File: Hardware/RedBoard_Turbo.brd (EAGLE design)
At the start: 58.4 x 53.3 mm, 144 parts, among them Q1 2.5A/30V, Q2 2N7002PW, U1 MCP73831, U2 74AHC1G125, U3 3.3V, U4 ATSAMD21G-A, U5 W25Q32FV, Y1 32.768kHz

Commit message: Added board title
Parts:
- added U$84: (no value), buzzard_labels (28):REDBOARD_TURBO0
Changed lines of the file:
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@@
 <element name="FID3" library="SparkFun-Aesthetics" package="FIDUCIAL-1X2" value="FIDUCIAL1X2" x="12.7" y="5.08" rot="MR0"/>
 <element name="FID4" library="SparkFun-Aesthetics" package="FIDUCIAL-1X2" value="FIDUCIAL1X2" x="50.8" y="43.18" rot="MR0"/>
+<element name="U$84" library="buzzard_labels (28)" package="REDBOARD_TURBO0" value="" x="12.319" y="24.13"/>
 </elements>
 <signals>

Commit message: Add testpoint and label for LED
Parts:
- added TP1: TEST-POINTTP_15TH_THRU, SparkFun-Connectors:TP_15TH
- added U$85: (no value), buzzard_labels (31):400
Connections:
- net RX_LED/SWDIO: now also TP1.P$1
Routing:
- net RX_LED/SWDIO: track 69.2 -> 71.4 mm
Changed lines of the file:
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@@
 <wire x1="53.086" y1="53.34" x2="-1.27" y2="53.34" width="0.2032" layer="20"/>
 <text x="3.81" y="48.26" size="1.016" layer="16" font="vector" ratio="15" rot="MR0" align="top-center">v01</text>
-<dimension x1="0" y1="0" x2="57.15" y2="5.08" x3="28.575" y3="-20.32" textsize="1.27" textratio="15" layer="47" dtype="horizontal" unit="inch" precision="3"/>
 <dimension x1="0" y1="0" x2="54.61" y2="7.62" x3="-5.08" y3="3.81" textsize="1.27" textratio="15" layer="47" dtype="vertical" unit="inch"/>
 <dimension x1="0" y1="0" x2="54.61" y2="35.56" x3="-7.62" y3="17.78" textsize="1.27" textratio="15" layer="47" dtype="vertical" unit="inch"/>
-<dimension x1="0" y1="0" x2="3.81" y2="50.8" x3="1.905" y3="-5.08" textsize="1.27" textratio="15" layer="47" dtype="horizontal" unit="inch" precision="3"/>
-<dimension x1="0" y1="0" x2="2.54" y2="2.54" x3="1.27" y3="-2.54" textsize="1.27" textratio="15" layer="47" dtype="horizontal" unit="inch" precision="3"/>
 <dimension x1="0" y1="0" x2="0" y2="53.34" x3="-12.7" y3="26.67" textsize="1.27" textratio="15" layer="47" dtype="vertical" unit="inch"/>
-<dimension x1="0" y1="0" x2="54.61" y2="35.56" x3="27.305" y3="-17.78" textsize="1.27" textratio="15" layer="47" dtype="horizontal" unit="inch" precision="3"/>
 <text x="34.29" y="-29.21" size="1.778" layer="51" font="vector" ratio="15">Jim Lindblom</text>
 <text x="44.958" y="46.609" size="1.27" layer="21" font="vector" ratio="15" rot="R90" align="center-right">~</text>
@@
 <text x="43.942" y="46.99" size="1.27" layer="22" font="vector" ratio="15" rot="MR90" align="center-right">~</text>
 <text x="-17.78" y="-8.89" size="1.27" layer="47" font="vector" ratio="15">Units in inches</text>
-<dimension x1="0" y1="0" x2="16.51" y2="2.54" x3="8.255" y3="-7.62" textsize="1.27" textratio="15" layer="47" dtype="horizontal" unit="inch" precision="3"/>
-<dimension x1="0" y1="0" x2="39.37" y2="2.54" x3="19.685" y3="-15.24" textsize="1.27" textratio="15" layer="47" dtype="horizontal" unit="inch" precision="3"/>
 <dimension x1="0" y1="0" x2="16.51" y2="2.54" x3="-1.27" y3="1.27" textsize="1.27" textratio="15" layer="47" dtype="vertical" unit="inch" precision="3"/>
 <dimension x1="0" y1="0" x2="7.366" y2="50.8" x3="-10.16" y3="25.4" textsize="1.27" textratio="15" layer="47" dtype="vertical" unit="inch" precision="3"/>
-<dimension x1="0" y1="0" x2="7.366" y2="50.8" x3="3.683" y3="-10.16" textsize="1.27" textratio="15" layer="47" dtype="horizontal" unit="inch" precision="3"/>
-<dimension x1="0" y1="0" x2="34.29" y2="50.8" x3="17.145" y3="-12.7" textsize="1.27" textratio="15" layer="47" dtype="horizontal" unit="inch" precision="3"/>
+<dimension x1="-1.27" y1="0" x2="2.54" y2="2.54" x3="0.635" y3="-3.81" textsize="1.27" textratio="15" layer="47" dtype="horizontal" unit="inch"/>
 </plain>
 <attributes>
@@
 <element name="FID4" library="SparkFun-Aesthetics" package="FIDUCIAL-1X2" value="FIDUCIAL1X2" x="50.8" y="43.18" rot="MR0"/>
 <element name="U$84" library="buzzard_labels (28)" package="REDBOARD_TURBO0" value="" x="12.319" y="24.13"/>
+<element name="TP1" library="SparkFun-Connectors" package="TP_15TH" value="TEST-POINTTP_15TH_THRU" x="41.275" y="19.685"/>
+<element name="U$85" library="buzzard_labels (31)" package="400" value="" x="34.163" y="40.132" rot="R90"/>
 </elements>
 <signals>
@@
 <wire x1="39.751" y1="18.161" x2="39.497" y2="18.415" width="0.2032" layer="1"/>
 <wire x1="39.497" y1="18.415" x2="38.735" y2="18.415" width="0.2032" layer="1"/>
+<contactref element="TP1" pad="P$1"/>
+<wire x1="39.751" y1="18.161" x2="41.275" y2="19.685" width="0.254" layer="1"/>
 </signal>
 <signal name="TX_LED">

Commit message: Changes from review
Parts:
- moved C11 1.27 mm to (33.0, 26.7)
- moved C3 1.27 mm to (18.2, 7.62)
- moved C6 1.27 mm to (45.8, 29.8)
- moved C7 1.27 mm to (47.6, 23.4)
- moved C9 1.27 mm to (45.1, 23.4)
- moved FID2 1.27 mm to (55.9, 3.81)
- moved FID4 1.27 mm to (52.1, 43.2)
- moved J2 1.27 mm to (53.3, 16.5)
- moved LOGO2 1.27 mm to (47.0, 8.26)
- moved R11 1.27 mm to (49.5, 16.5)
- moved TP1 1.27 mm to (42.5, 19.7)
- moved U$10 1.27 mm to (40.6, 47.0)
- moved U$11 1.27 mm to (38.1, 47.0)
- moved U$12 1.27 mm to (35.6, 47.0)
- moved U$28 1.27 mm to (51.4, 14.1)
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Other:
- board text added: "Revised by Mike Hord"
- board text added: "v11"
- board text removed: "v01"

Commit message: Add polarity markings to JST connector
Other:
- board text added: "+"
- board text added: "-"
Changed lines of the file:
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@@
 <dimension x1="0" y1="0" x2="58.42" y2="5.08" x3="29.21" y3="-8.89" textsize="1.27" textratio="15" layer="47" dtype="horizontal" unit="inch"/>
 <text x="15.24" y="-31.75" size="1.778" layer="51" font="vector" ratio="15">Revised by Mike Hord</text>
+<text x="7.874" y="19.558" size="1.27" layer="21" font="vector" ratio="15">+</text>
+<text x="7.874" y="17.272" size="1.27" layer="21" font="vector" ratio="15">-</text>
 </plain>
 <attributes>
@@
 <element name="JP6" library="samd21-temp" package="2X5-PTH-1.27MM" value="CORTEX_DEBUGPTH" x="39.37" y="15.875" rot="R270"/>
 <element name="L1" library="SparkFun-Passives" package="0603" value="FB - 30Ohm" x="47.117" y="29.845" rot="R90">
-<attribute name="PROD_ID" value="RES-07859" x="47.117" y="29.845" size="1.778" layer="27" rot="R90" display="off"/>
+<attribute name="PROD_ID" value="NDUC-07859" x="47.117" y="29.845" size="1.778" layer="27" rot="R90" display="off"/>
 </element>
 <element name="LOGO3" library="SparkFun-Aesthetics" package="OSHW-LOGO-S" value="OSHW-LOGOS" x="42.799" y="10.668"/>

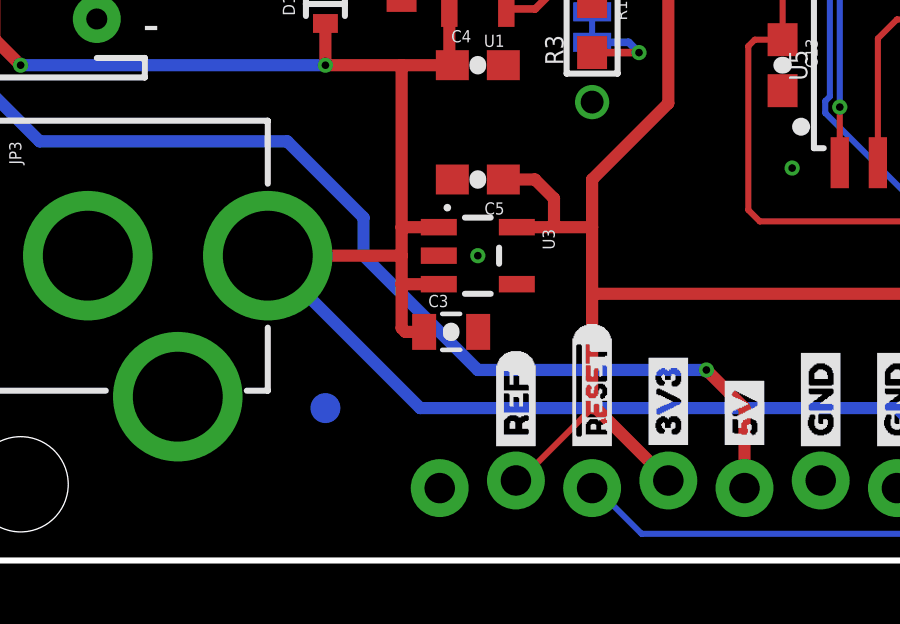
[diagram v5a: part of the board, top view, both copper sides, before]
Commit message: Updated 0805 cap, approved DRC errors
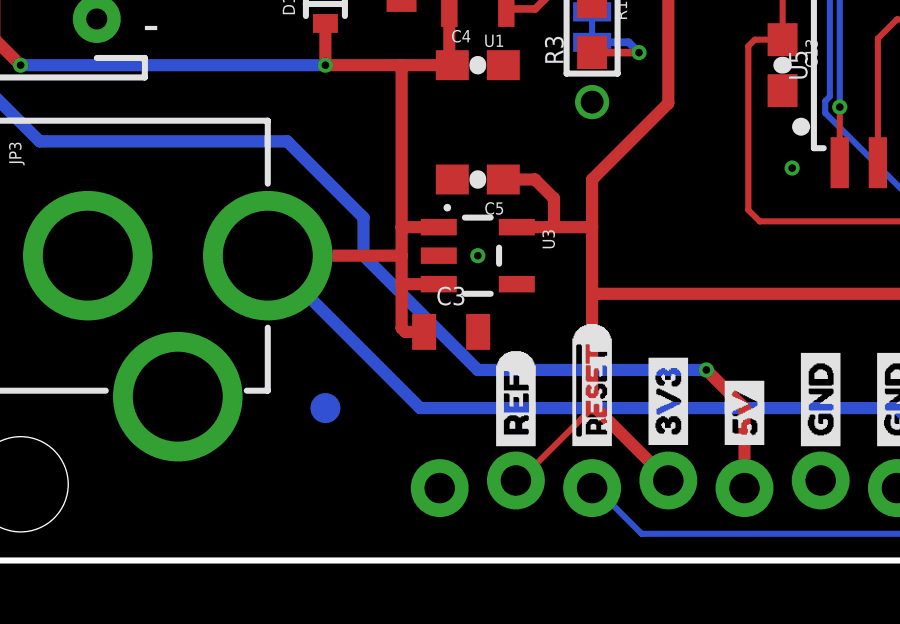
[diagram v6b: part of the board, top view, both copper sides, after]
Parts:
- C1: device SparkFun-Capacitors:1206 -> SparkFun-Capacitors:1206@1
- C3: device SparkFun-Capacitors:0805-CAP -> SparkFun-Capacitors:0805
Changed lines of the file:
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@@
 <?xml version="1.0" encoding="utf-8"?>
 <!DOCTYPE eagle SYSTEM "eagle.dtd">
-<eagle version="9.0.1">
+<eagle version="8.7.0">
 <drawing>
 <settings>
@@
 <layers>
 <layer number="1" name="Top" color="4" fill="1" visible="yes" active="yes"/>
-<layer number="2" name="Route2" color="1" fill="3" visible="no" active="yes"/>
-<layer number="15" name="Route15" color="4" fill="6" visible="no" active="yes"/>
 <layer number="16" name="Bottom" color="1" fill="1" visible="yes" active="yes"/>
 <layer number="17" name="Pads" color="2" fill="1" visible="yes" active="yes"/>
@@
 <layer number="19" name="Unrouted" color="6" fill="1" visible="yes" active="yes"/>
 <layer number="20" name="Dimension" color="15" fill="1" visible="yes" active="yes"/>
-<layer number="21" name="tPlace" color="16" fill="1" visible="yes" active="yes"/>
-<layer number="22" name="bPlace" color="14" fill="1" visible="yes" active="yes"/>
+<layer number="21" name="tPlace" color="16" fill="1" visible="no" active="yes"/>
+<layer number="22" name="bPlace" color="14" fill="1" visible="no" active="yes"/>
 <layer number="23" name="tOrigins" color="15" fill="1" visible="yes" active="yes"/>
 <layer number="24" name="bOrigins" color="15" fill="1" visible="yes" active="yes"/>
@@
 <layer number="31" name="tCream" color="7" fill="5" visible="no" active="yes"/>
 <layer number="32" name="bCream" color="7" fill="4" visible="no" active="yes"/>
+<layer number="33" name="tFinish" color="6" fill="3" visible="no" active="yes"/>
+<layer number="34" name="bFinish" color="6" fill="6" visible="no" active="yes"/>
+<layer number="35" name="tGlue" color="7" fill="4" visible="no" active="yes"/>
+<layer number="36" name="bGlue" color="7" fill="5" visible="no" active="yes"/>
+<layer number="37" name="tTest" color="7" fill="1" visible="no" active="yes"/>
+<layer number="38" name="bTest" color="7" fill="1" visible="no" active="yes"/>
 <layer number="39" name="tKeepout" color="4" fill="11" visible="no" active="yes"/>
 <layer number="40" name="bKeepout" color="1" fill="11" visible="no" active="yes"/>
@@
 <layer number="48" name="Document" color="7" fill="1" visible="no" active="yes"/>
 <layer number="49" name="Reference" color="7" fill="1" visible="no" active="yes"/>
+<layer number="50" name="dxf" color="7" fill="1" visible="no" active="yes"/>
 <layer number="51" name="tDocu" color="6" fill="1" visible="yes" active="yes"/>
 <layer number="52" name="bDocu" color="6" fill="1" visible="no" active="yes"/>
+<layer number="91" name="Nets" color="2" fill="1" visible="no" active="no"/>
+<layer number="92" name="Busses" color="1" fill="1" visible="no" active="no"/>
+<layer number="93" name="Pins" color="2" fill="1" visible="no" active="no"/>
+<layer number="94" name="Symbols" color="4" fill="1" visible="no" active="no"/>
+<layer number="95" name="Names" color="7" fill="1" visible="no" active="no"/>
+<layer number="96" name="Values" color="7" fill="1" visible="no" active="no"/>
+<layer number="2" name="Route2" color="1" fill="3" visible="no" active="no"/>
+<layer number="15" name="Route15" color="4" fill="6" visible="no" active="no"/>
 <layer number="3" name="Route3" color="4" fill="3" visible="no" active="no"/>
 <layer number="4" name="Route4" color="1" fill="4" visible="no" active="no"/>
@@
 <layer number="13" name="Route13" color="4" fill="5" visible="no" active="no"/>
 <layer number="14" name="Route14" color="1" fill="6" visible="no" active="no"/>
-<layer number="33" name="tFinish" color="6" fill="3" visible="no" active="no"/>
-<layer number="34" name="bFinish" color="6" fill="6" visible="no" active="no"/>
-<layer number="35" name="tGlue" color="7" fill="4" visible="no" active="no"/>
-<layer number="36" name="bGlue" color="7" fill="5" visible="no" active="no"/>
-<layer number="37" name="tTest" color="7" fill="1" visible="no" active="no"/>
-<layer number="38" name="bTest" color="7" fill="1" visible="no" active="no"/>
-<layer number="50" name="dxf" color="7" fill="1" visible="no" active="no"/>
 <layer number="53" name="tGND_GNDA" color="7" fill="9" visible="no" active="no"/>
 <layer number="54" name="bGND_GNDA" color="1" fill="9" visible="no" active="no"/>
@@
 <layer number="89" name="SimProbes" color="9" fill="1" visible="no" active="no"/>
 <layer number="90" name="Modules" color="5" fill="1" visible="no" active="no"/>
-<layer number="91" name="Nets" color="2" fill="1" visible="no" active="no"/>
-<layer number="92" name="Busses" color="1" fill="1" visible="no" active="no"/>
-<layer number="93" name="Pins" color="2" fill="1" visible="no" active="no"/>
-<layer number="94" name="Symbols" color="4" fill="1" visible="no" active="no"/>
-<layer number="95" name="Names" color="7" fill="1" visible="no" active="no"/>
-<layer number="96" name="Values" color="7" fill="1" visible="no" active="no"/>
 <layer number="97" name="Info" color="7" fill="1" visible="no" active="no"/>
 <layer number="98" name="Guide" color="6" fill="1" visible="no" active="no"/>
@@
 <attribute name="VALUE" value="15pF" x="47.625" y="23.368" size="1.778" layer="27" rot="R270" display="off"/>
 </element>
-<element name="C3" library="SparkFun-Capacitors" package="0805-CAP" value="1.0uF" x="18.161" y="7.62">
-<attribute name="PROD_ID" value="CAP-11625" x="18.161" y="7.62" size="1.778" layer="27" display="off"/>
+<element name="C3" library="SparkFun-Capacitors" package="0805" value="1.0uF" x="18.161" y="7.62">
+<attribute name="PROD_ID" value="CAP-08064" x="18.161" y="7.62" size="1.778" layer="27" display="off"/>
 <attribute name="VALUE" value="1.0uF" x="18.161" y="7.62" size="1.778" layer="27" display="off"/>
 </element>
@@
 <attribute name="PROD_ID" value="CAP-00810" x="40.894" y="36.83" size="1.778" layer="27" font="vector" ratio="15" rot="R180" display="off"/>
 </element>
-<element name="C1" library="SparkFun-Capacitors" package="1206" value="2.2UF" x="11.43" y="43.18" rot="R270">
+<element name="C1" library="SparkFun-Capacitors" package="1206@1" value="2.2UF" x="11.43" y="43.18" rot="R270">
 <attribute name="PROD_ID" value="CAP-10009" x="11.43" y="43.18" size="1.778" layer="27" font="vector" ratio="15" rot="R270" display="off"/>
 </element>

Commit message: v20
Updated silk
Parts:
- removed SJ1: R-prog, SparkFun-Passives:PAD-JUMPER-2-NC_BY_TRACE_YES_SILK
- removed U$74: (no value), buzzard_labels (25):LED_EN36
- added U$86: (no value), bitmap#jpg:BITMAP#JPG
- added U$87: (no value), buzzard_labels (1):CHG_SET1
- LOGO2: value SFE_LOGO_NAME_FLAME.4_INCH -> SFE_LOGO_NAME_FLAME.3_INCH; device SparkFun-Aesthetics:SFE_LOGO_NAME_FLAME_.4 -> SparkFun-Aesthetics:SFE_LOGO_NAME_FLAME_.3
- U$54: device buzzard_labels (25):CHG_SET35 -> buzzard_labels (1):LED_EN0
- U$84: device buzzard_labels (28):REDBOARD_TURBO0 -> buzzard_labels:440
- U$85: device buzzard_labels (31):400 -> buzzard_labels:REDBOARD_TURBO1
- moved LOGO2 33.3 mm to (19.3, 26.7), turned to 270 degrees
- moved U$84 27.2 mm to (35.6, 40.1), turned to 90 degrees
- moved U$54 23.9 mm to (4.32, 38.2)
- moved LOGO1 12.4 mm to (22.9, 28.8)
- moved R6 8.91 mm to (3.81, 23.5), turned to 180 degrees
- moved LOGO4 8.84 mm to (26.7, 26.7), turned to 270 degrees
- moved U$85 5.51 mm to (34.0, 45.5), flipped to the bottom, turned to 270 degrees
- moved FID1 4.02 mm to (1.27, 52.1)
- moved C4 0.51 mm to (19.1, 16.0)
- moved R2 0.25 mm to (16.5, 37.1)
- moved S1 0.13 mm to (48.3, 10.3)
- moved C3 0.13 mm to (18.2, 7.49)
- moved U$83 0.13 mm to (45.7, 12.7)
- turned R1 to 90 degrees
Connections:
- removed net N$15: R3.2, SJ1.2, U1.5
- net N$13: now also R3.2, U1.5; no longer SJ1.1
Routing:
- net CHG_STAT: track 7.77 -> 19.6 mm
- net 3.3V: track 237.2 -> 230.3 mm
- net N$8: track 7.95 -> 1.28 mm
- net N$15: track 5.64 -> 0.00 mm
- net D13: track 65.4 -> 60.3 mm
- net D2: track 20.6 -> 24.9 mm
- net GND: track 34.7 -> 37.6 mm, vias 22 -> 50
- net N$13: track 3.27 -> 5.87 mm, vias 1 -> 0
- net VIN: track 125.7 -> 127.8 mm
- net USB_HOST_EN: track 32.2 -> 30.3 mm
- net FLASH_MISO: track 18.9 -> 20.7 mm
- net RX_LED/SWDIO: track 71.4 -> 72.7 mm
- net VBAT: track 14.1 -> 15.3 mm
- net SPI_MISO: track 25.6 -> 24.7 mm
- net LED/SWCLK: track 31.6 -> 32.6 mm
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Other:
- board text added: "v20"
- board text removed: "v11"

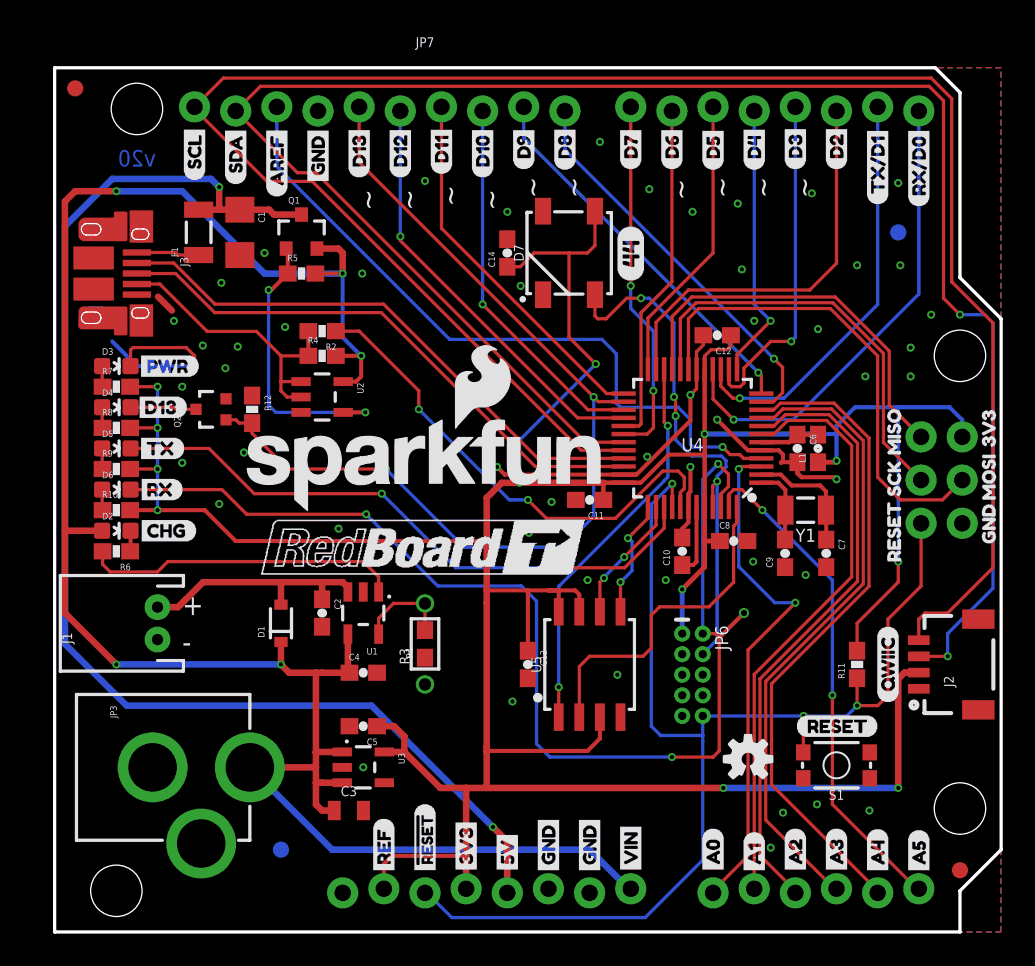
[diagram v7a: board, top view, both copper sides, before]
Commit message: Design Review Changes
- Switched board version to v10
- Changed RED charge LED to yellow
- Updated power LED silk
- Added barrel jack max voltage silk
- Replaced reset button with larger button and longer actuator
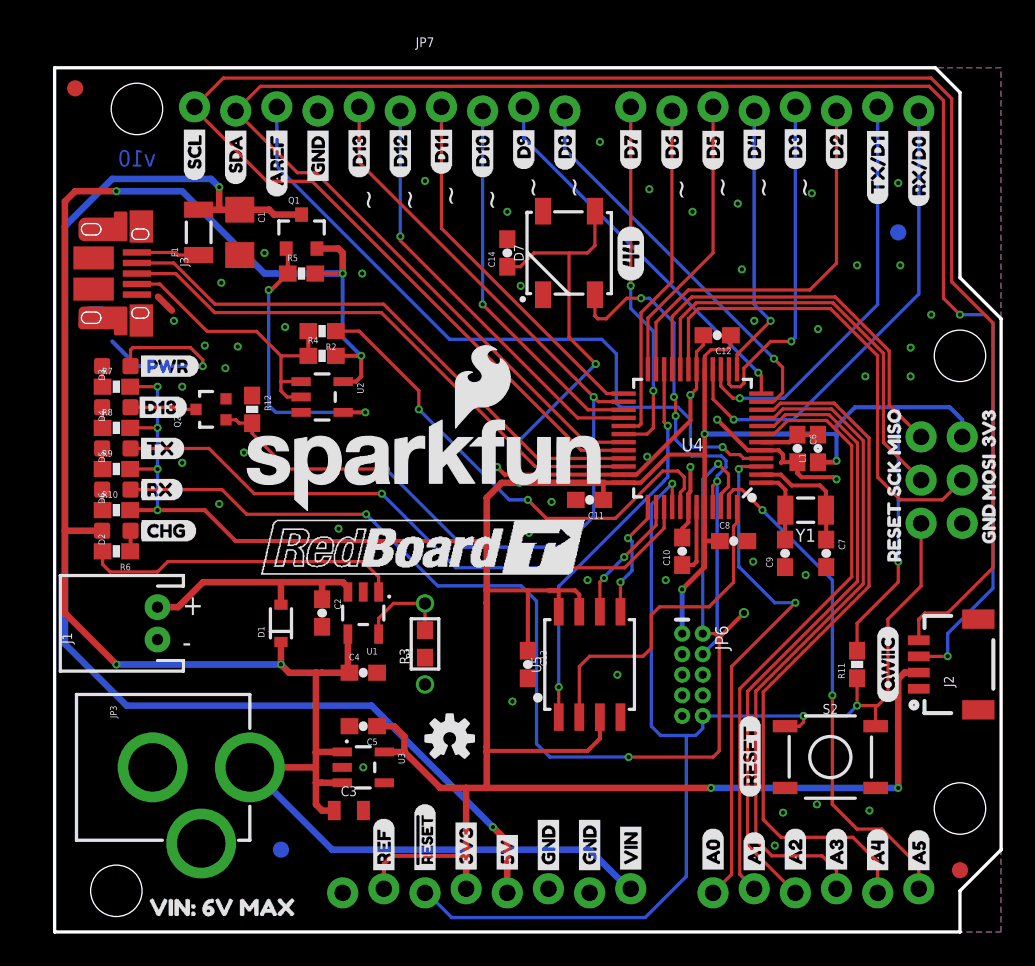
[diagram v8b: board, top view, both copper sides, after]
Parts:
- removed S1: RESET, SparkFun-Switches:TACTILE_SWITCH_SMD_4.6X2.8MM
- added S2: (no value), SparkFun-Switches:TACTILE_SWITCH_SMD_5.2MM
- added U$74: (no value), buzzard_labels:PWR0
- added U$88: (no value), buzzard_labels:VIN#_6V_MAX2
- D2: value RED -> Yellow
- U$54: device buzzard_labels (1):LED_EN0 -> buzzard_labels:LED1
- moved LOGO3 18.5 mm to (24.4, 11.9)
- moved U$83 5.25 mm to (42.9, 8.26), turned to 90 degrees
- moved U$54 4.07 mm to (8.26, 37.2)
- turned D2 to 0 degrees
- turned D3 to 0 degrees
- turned D4 to 0 degrees
- turned D5 to 0 degrees
- turned D6 to 0 degrees
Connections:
- net !RESET: now also S2.1, S2.2; no longer S1.2
- net GND: now also S2.3, S2.4; no longer S1.3
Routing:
- net A4: track 41.0 -> 44.0 mm
- net A3: track 39.4 -> 41.6 mm
- net A5: track 30.9 -> 32.8 mm
- net N$12: track 7.63 -> 8.50 mm
- net A1: track 36.4 -> 37.2 mm
- net A2: track 38.1 -> 38.7 mm
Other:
- board text added: "v10"
- board text removed: "v20"
